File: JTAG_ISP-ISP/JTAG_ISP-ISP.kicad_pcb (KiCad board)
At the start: 2 copper layers, 23.1 x 46.1 mm, 9 parts, among them J1 Conn_02x03_Odd_Even, J2 Conn_01x08, J3 Conn_01x08

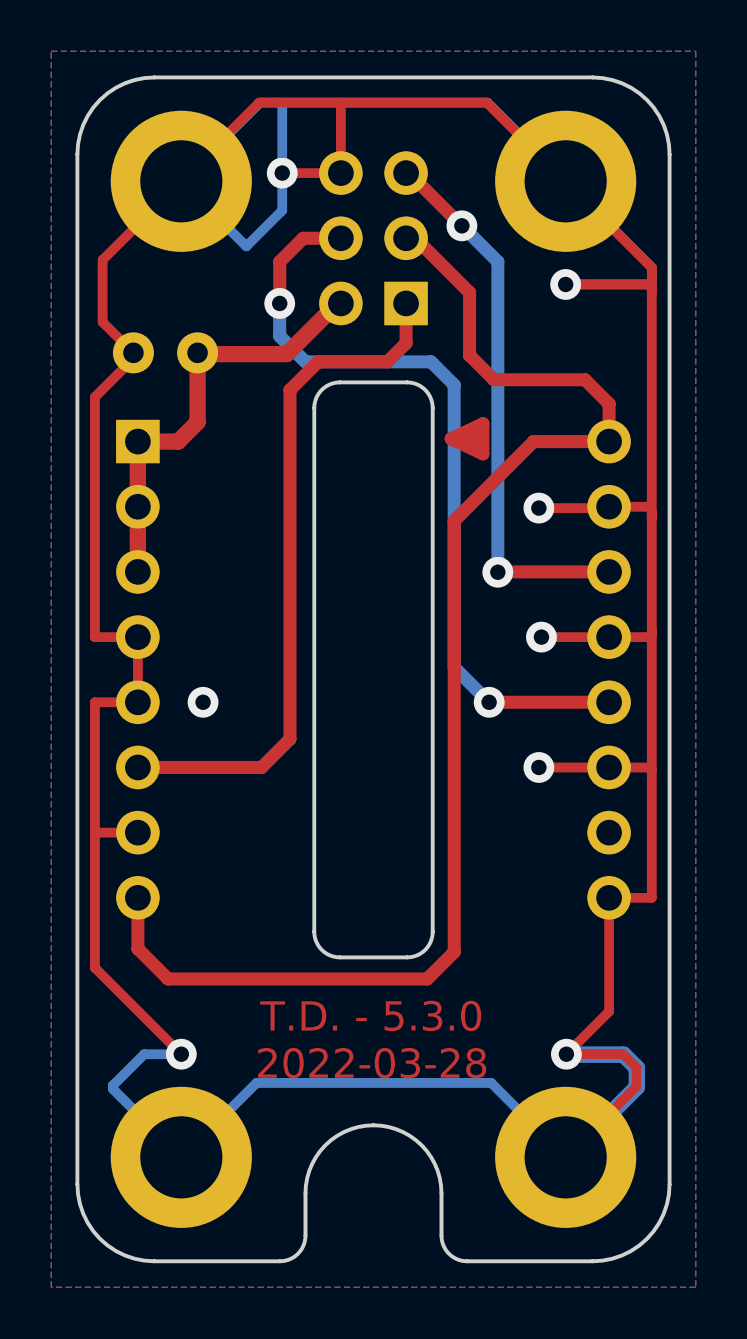
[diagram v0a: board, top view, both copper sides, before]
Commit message: **# [PCB]** + Ajout silkscreen autour du trou pour le connecteur HDR; * Alignement des silkscreen pour le nom des pièces; * Flèche indiquant la broche #1 est transférée sur le silkscreen; * Reroutage du ground; * Suppression de vias inutiles; * Mise à jour des fichiers gerbers; * Mise à jour de la cartouche;     * Date actuelle;     * Version actuelle.
**# [SCHÉMA]**
* Mise à jour de la cartouche;
    * Date actuelle;
    * Version actuelle.
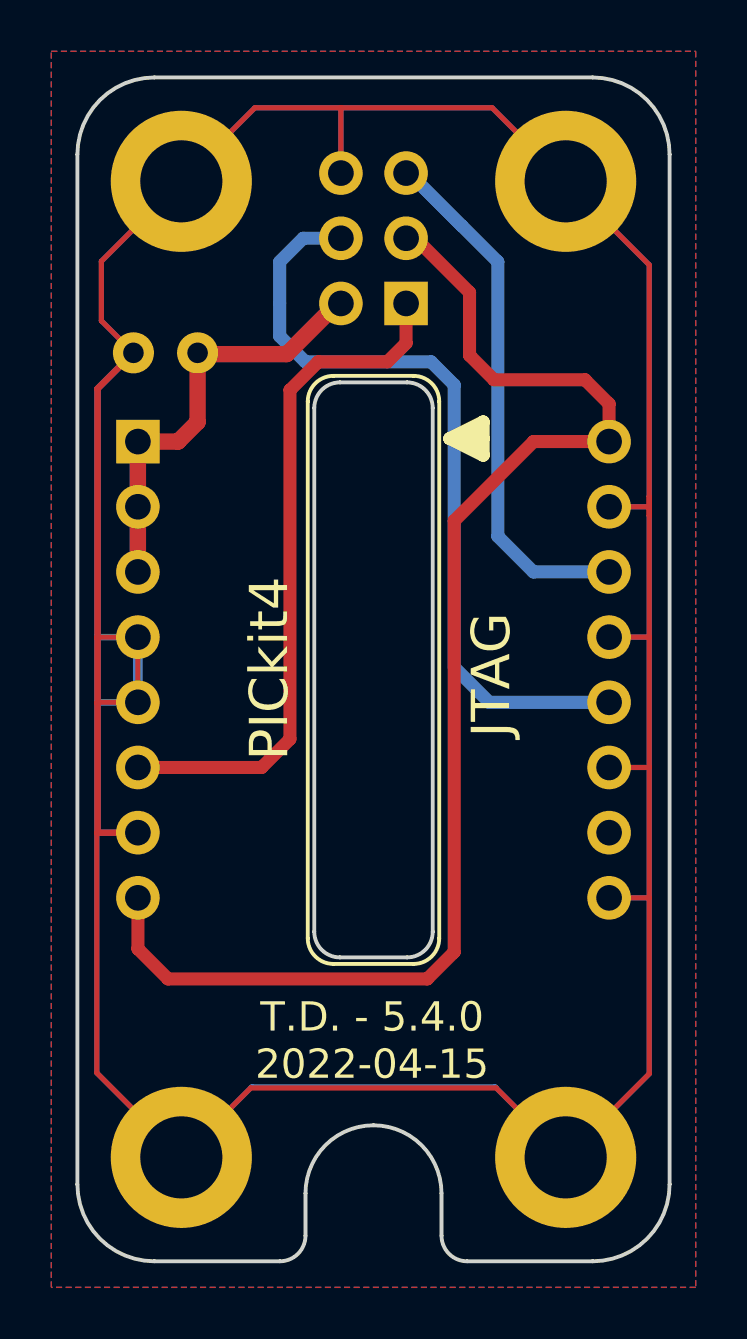
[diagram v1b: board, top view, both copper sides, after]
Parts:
- removed the REF** at (115.7, 59.0)
- added REF**: Fleche_small-silkscreen, THOMAS_library:Fleche_small-silkscreen, F.Cu at (115.7, 59.0)
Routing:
- net GND: track 195.2 -> 269.6 mm, vias 8 -> 0
- net +5V: track 16.7 -> 21.8 mm
- net RESET: track 21.4 -> 20.5 mm, vias 2 -> 0
- net MOSI: vias 2 -> 0
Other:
- board text added: "JTAG"
- board text added: "PICkit4"
- board text added: "T.D. - 5.4.0 2022-04-15"
- board text removed: "T.D. - 5.3.0 2022-03-28"

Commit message: **# [PCB]** + Création d'une version avec des composants montés en surface à partir de la version précédente.
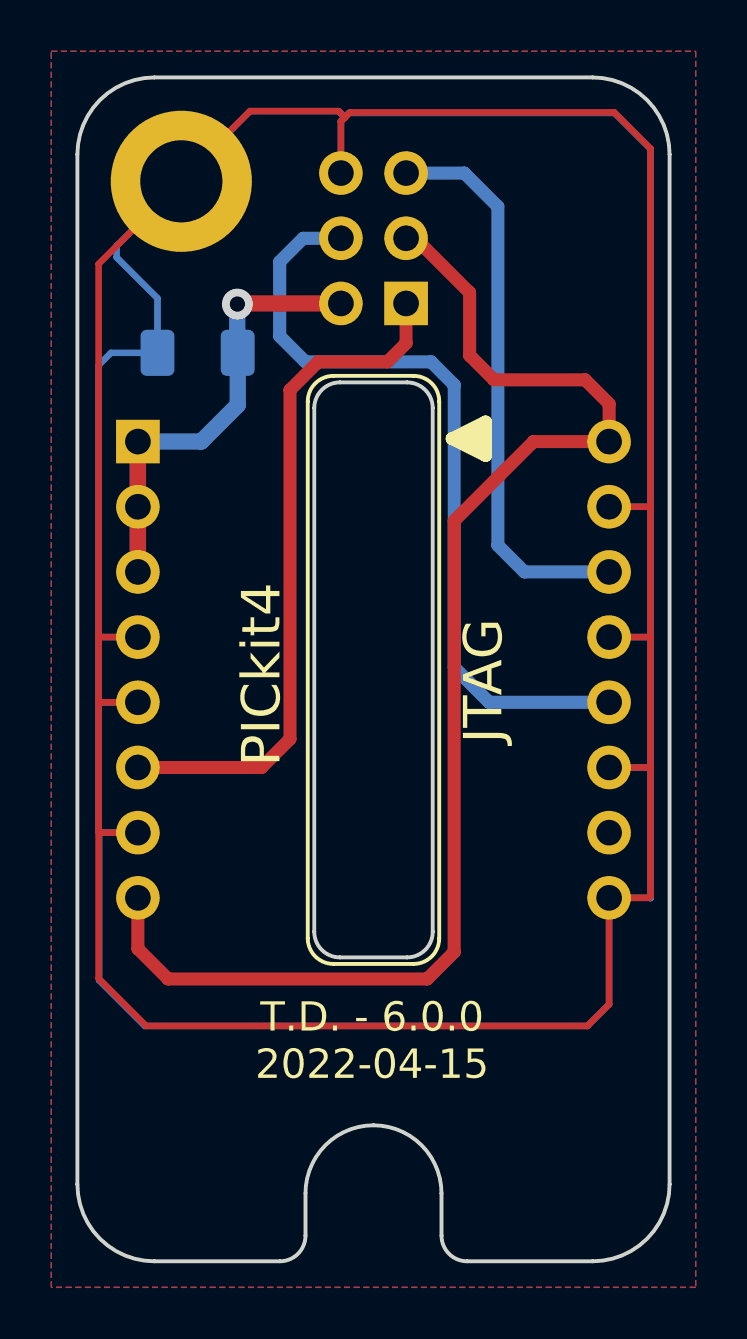
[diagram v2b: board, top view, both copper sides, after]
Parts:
- removed the REF** at (104.0, 87.4)
- removed the REF** at (119.0, 49.3)
- removed the REF** at (119.0, 87.4)
- C1: footprint Capacitor_THT:C_Disc_D3.0mm_W2.0mm_P2.50mm -> Capacitor_SMD:C_1206_3216Metric_Pad1.33x1.80mm_HandSolder
- moved REF** 0.09 mm to (115.8, 59.0)
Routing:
- net GND: track 269.6 -> 242.9 mm
- net RESET: track 20.5 -> 22.1 mm
- net +5V: track 21.8 -> 22.7 mm, vias 0 -> 1
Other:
- board text added: "T.D. - 6.0.0 2022-04-15"
- board text removed: "T.D. - 5.4.0 2022-04-15"
